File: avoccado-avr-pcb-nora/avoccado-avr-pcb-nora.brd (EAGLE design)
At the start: 50 x 50 mm, 51 parts, among them Q1 16MHz, Q2 FET, U2 MCP73831

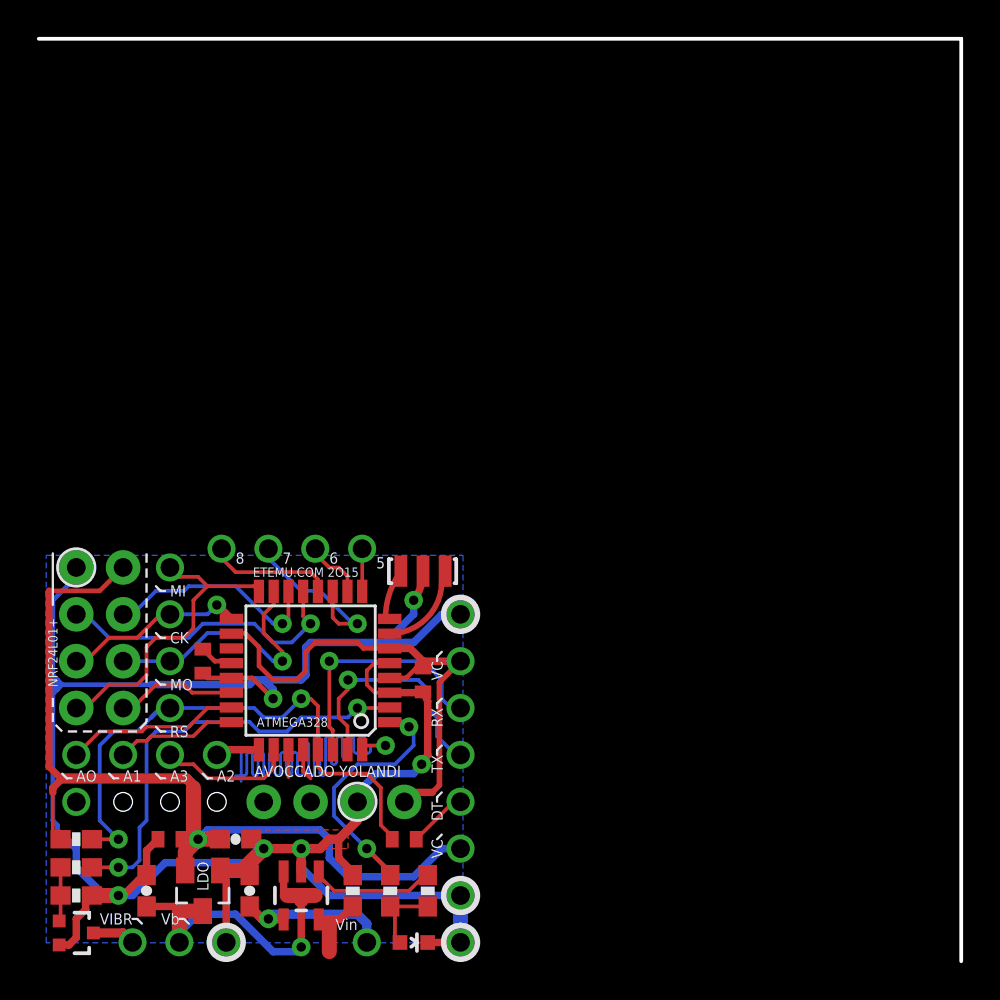
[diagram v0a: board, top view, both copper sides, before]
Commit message: add rectangles at plated half holes
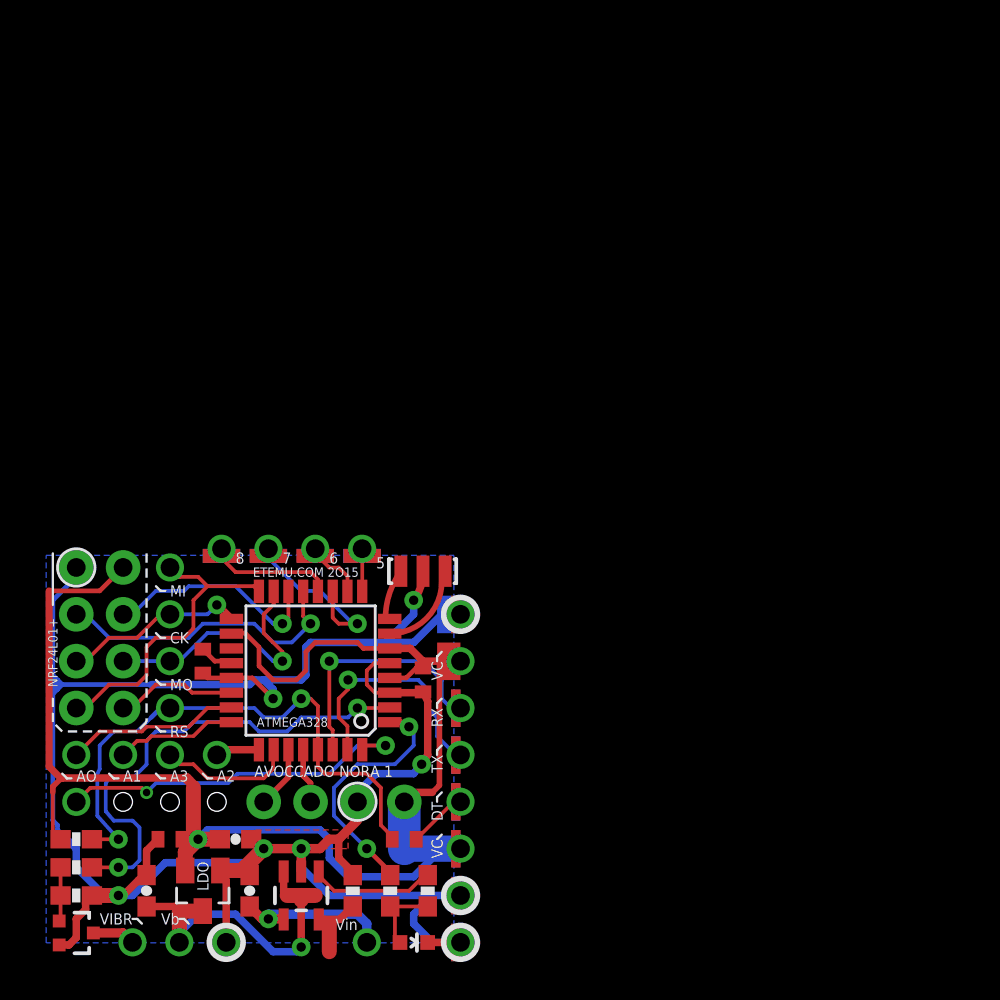
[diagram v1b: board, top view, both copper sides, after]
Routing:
- net D2: track 38.6 -> 19.6 mm, vias 1 -> 2
- net 3.3V: track 77.5 -> 83.4 mm
- net D4: track 23.7 -> 26.5 mm
- net GND: track 124.5 -> 126.8 mm
- net A4: track 1.48 -> 3.38 mm
- net A5: track 1.72 -> 2.99 mm
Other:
- board outline removed
- board text added: "AVOCCADO NORA 1"
- board text removed: "AVOCCADO YOLANDI"

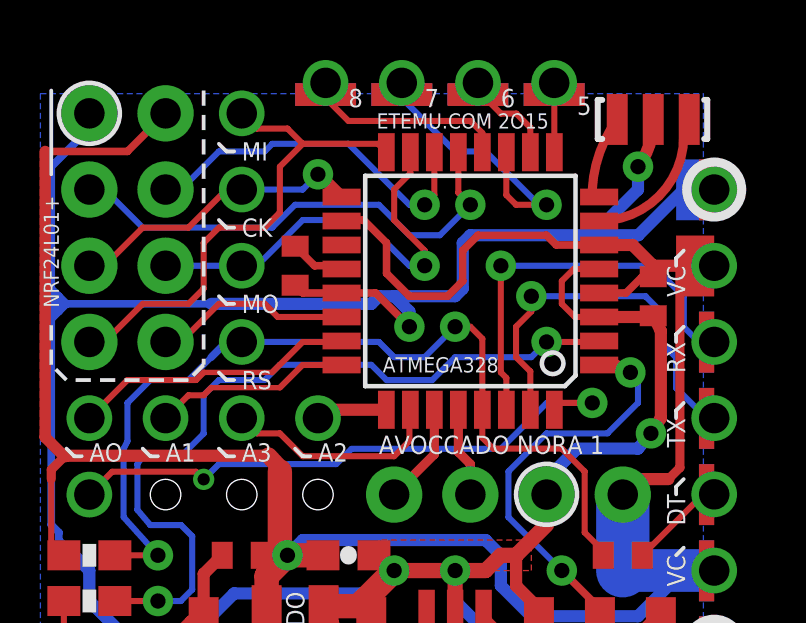
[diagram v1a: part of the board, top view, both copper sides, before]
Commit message: panelized nora to 50x50mm²
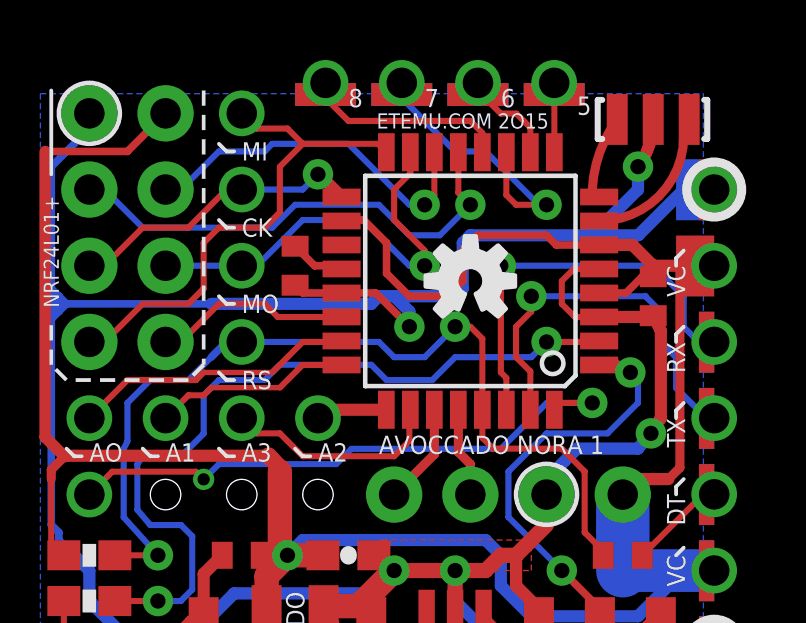
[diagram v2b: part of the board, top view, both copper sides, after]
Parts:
- added LOGO2: OSHW-LOGOS, SparkFun-Aesthetics:OSHW-LOGO-S
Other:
- board text removed: "ATMEGA328"
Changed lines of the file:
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@@
 Yolandi is the minified version of Avoccado-avr with less pins broken out and a footprint of less than one square inch for the PCB without peripherals.</description>
 <plain>
-<text x="11.811" y="12.708" size="0.508" layer="21" font="vector">ATMEGA328</text>
 <circle x="17.78" y="6.104" radius="0.254" width="0.508" layer="30"/>
 <circle x="4.318" y="5.088" radius="0.254" width="0.508" layer="30"/>
@@
 <element name="JP5" library="SparkFun-Connectors" package="1X02_NO_SILK" value="M021X02_NO_SILK" x="14.732" y="8.636" smashed="yes" rot="R180"/>
 <element name="TP2" library="SparkFun-Connectors" package="1X01NS-KIT" value="M01NOSILK-KIT" x="2.032" y="8.636" smashed="yes"/>
+<element name="LOGO2" library="SparkFun-Aesthetics" package="OSHW-LOGO-S" value="OSHW-LOGOS" x="14.732" y="15.756"/>
 </elements>
 <signals>
